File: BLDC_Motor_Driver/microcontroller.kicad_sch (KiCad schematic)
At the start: 27 parts, among them J101 USB4105-GF-A, J102 Conn_01x05, SW101 SW_Push, SW102 SW_Push, U103 STM32L412CBTx, U105 ECMF02-2AMX6

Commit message: finished power circuitry
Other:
- company: (none) -> University of Illinois Urbana-Champaign
- title: (none) -> BLDC Motor Inverter Microcontroller Circuitry
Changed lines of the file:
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@@
 	(generator_version "9.0")
 	(paper "A4")
+	(title_block
+		(title "BLDC Motor Inverter Microcontroller Circuitry")
+		(rev "A")
+		(company "University of Illinois Urbana-Champaign")
+		(comment 4 "Contributors: Thomas McManamen, Noah Breit")
+	)
 	(rectangle
 		(start 93.98 15.24)

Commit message: hall effect done, adding testpoints/connectors
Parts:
- added J601, J602: Conn_01x05, Connector_PinHeader_2.54mm:PinHeader_1x05_P2.54mm_Vertical, symbol Connector_Generic:Conn_01x05
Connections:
- net +3V3: now also J601.1 (Pin_1), J602.1 (Pin_1)
- net GND: now also J601.5 (Pin_5), J602.5 (Pin_5)
- net SPI1_MISO: now also J601.3 (Pin_3)
- net SPI1_MOSI: now also J601.4 (Pin_4)
- net SPI1_SCK: now also J601.2 (Pin_2)
- net SPI2_MISO: now also J602.3 (Pin_3)
- net SPI2_MOSI: now also J602.4 (Pin_4)
- net SPI2_SCK: now also J602.2 (Pin_2)
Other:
- note added: "Connectivity"
- note added: "add others"

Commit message: new GateDriver subsheet. reorg connectors to root sheet
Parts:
- removed C116, C117: 100nF, Capacitor_SMD:C_0603_1608Metric, symbol Device:C
- removed D102: RED LED, LED_SMD:LED_0603_1608Metric, symbol Device:LED
- removed D103: ORANGE LED, LED_SMD:LED_0603_1608Metric, symbol Device:LED
- removed D104: GREEN LED, LED_SMD:LED_0603_1608Metric, symbol Device:LED
- removed D105: BLUE LED, LED_SMD:LED_0603_1608Metric, symbol Device:LED
- removed J101: USB4105-GF-A, Connector_USB:USB_C_Receptacle_GCT_USB4105-xx-A_16P_TopMnt_Horizontal, symbol Connector:USB_C_Receptacle_USB2.0
- removed J102, J601, J602: Conn_01x05, Connector_PinHeader_2.54mm:PinHeader_1x05_P2.54mm_Vertical, symbol Connector_Generic:Conn_01x05
- removed R103: 10k, Resistor_SMD:R_0603_1608Metric, symbol Device:R_US
- removed R104, R105: 5.1k, Resistor_SMD:R_0603_1608Metric, symbol Device:R_US
- removed R107, R108, R109, R110: 470, Resistor_SMD:R_0603_1608Metric, symbol Device:R_US
- removed SW101, SW102: SW_Push, Button_Switch_SMD:SW_SPST_FSMSM, symbol Switch:SW_Push
- removed U105: ECMF02-2AMX6, Package_DFN_QFN:ST_UQFN-6L_1.5x1.7mm_P0.5mm, symbol Power_Protection:ECMF02-2AMX6
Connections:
- net +3V3 renamed 3.3V_REG
- no-connect marks 6 -> 3
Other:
- note removed: "Connectivity"
- note removed: "Debug LEDs"
- note removed: "Power/Serial"
- note removed: "Programming"
- note removed: "USB-C Port"
- note removed: "add others"

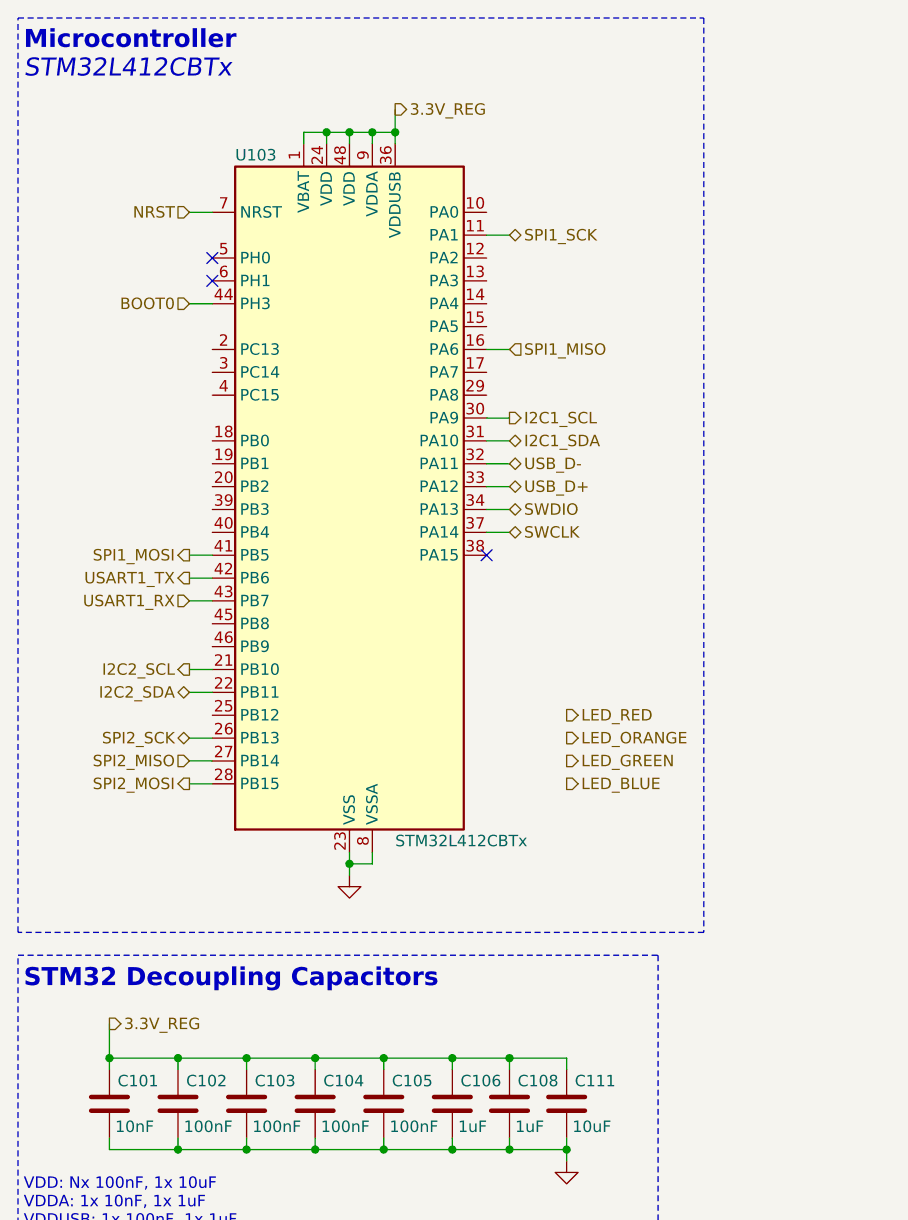
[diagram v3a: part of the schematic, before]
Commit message: added breakout connector and reformatted some things
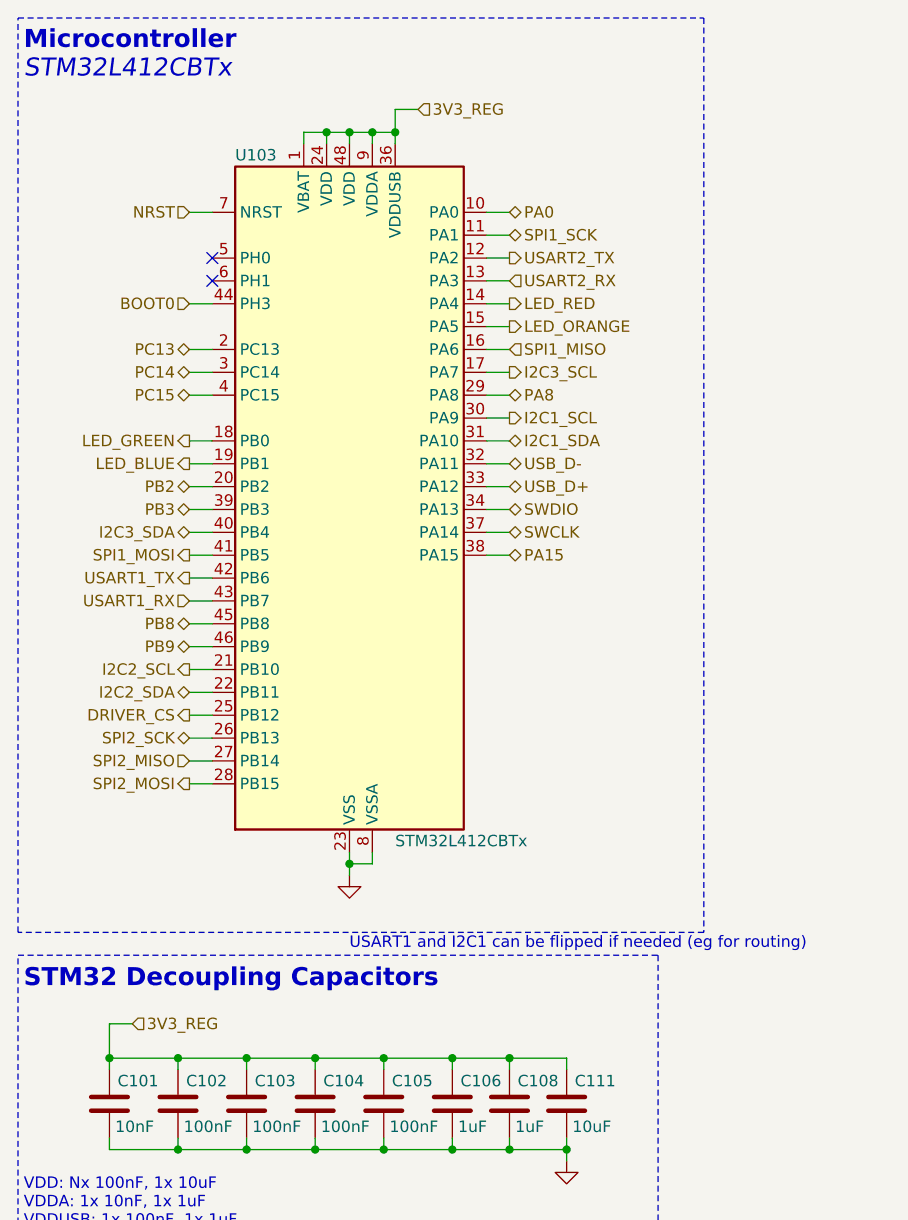
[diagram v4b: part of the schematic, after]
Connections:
- net LED_BLUE: now also U103.19 (PB1)
- net LED_GREEN: now also U103.18 (PB0)
- net LED_ORANGE: now also U103.15 (PA5)
- net LED_RED: now also U103.14 (PA4)
- net PA0: now reaches U103.10 (PA0)
- net USART2_TX: now reaches U103.12 (PA2)
- net USART2_RX: now reaches U103.13 (PA3)
- net I2C3_SCL: now reaches U103.17 (PA7)
- net PC13: now reaches U103.2 (PC13)
- net PB2: now reaches U103.20 (PB2)
- net DRIVER_CS: now reaches U103.25 (PB12)
- net PA8: now reaches U103.29 (PA8)
- net PC14: now reaches U103.3 (PC14)
- net PA15: now reaches U103.38 (PA15)
- net PB3: now reaches U103.39 (PB3)
- net PC15: now reaches U103.4 (PC15)
- net I2C3_SDA: now reaches U103.40 (PB4)
- net PB8: now reaches U103.45 (PB8)
- net PB9: now reaches U103.46 (PB9)
- net 3.3V_REG renamed 3V3_REG
- no-connect marks 3 -> 2
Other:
- note added: "USART1 and I2C1 can be flipped if needed (eg for routing)"

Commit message: schematics more or less done
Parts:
- renumbered C101 to C201, C102 to C202, C103 to C203, C104 to C204, C105 to C205, C106 to C206, C108 to C207, C111 to C208, U103 to U201
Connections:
- net 3V3_REG: no longer U201.1 (VBAT), U201.24 (VDD), U201.36 (VDDUSB), U201.48 (VDD), U201.9 (VDDA)
- new net +3V3: U201.1 (VBAT), U201.24 (VDD), U201.36 (VDDUSB), U201.48 (VDD), U201.9 (VDDA)

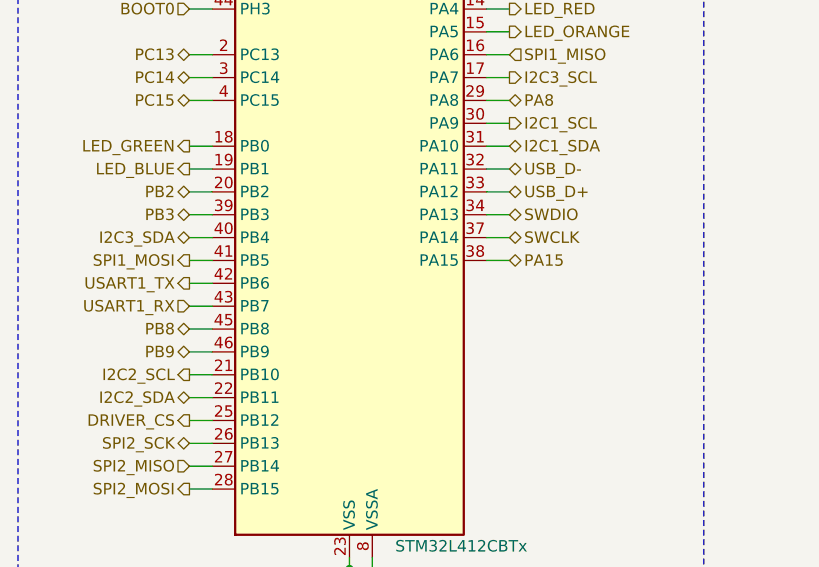
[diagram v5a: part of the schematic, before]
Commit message: wired driver rst/status ios to mcu, layout setup
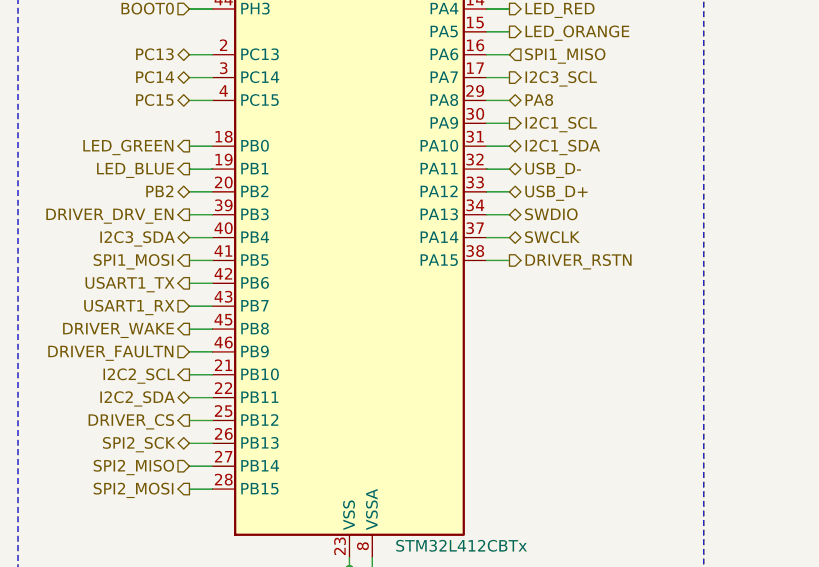
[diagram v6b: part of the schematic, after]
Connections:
- net PA15 renamed DRIVER_RSTN
- net PB3 renamed DRIVER_DRV_EN
- net PB8 renamed DRIVER_WAKE
- net PB9 renamed DRIVER_FAULTN
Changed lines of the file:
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@@
+		)
+	)
+	(hierarchical_label "DRIVER_DRV_EN"
+		(shape output)
+		(at 34.29 69.85 180)
+		(effects
+			(font
+				(size 1.27 1.27)
+			)
+			(justify right)
 		)
 	)
@@
 		)
 	)
-	(hierarchical_label "PB3"
-		(shape bidirectional)
-		(at 34.29 69.85 180)
-		(effects
-			(font
-				(size 1.27 1.27)
-			)
-			(justify right)
-		)
-	)
 	(hierarchical_label "DRIVER_CS"
 		(shape output)
@@
 		)
 	)
+	(hierarchical_label "DRIVER_RSTN"
+		(shape output)
+		(at 69.85 74.93 0)
+		(effects
+			(font
+				(size 1.27 1.27)
+			)
+			(justify left)
+		)
+	)
 	(hierarchical_label "SPI1_MISO"
 		(shape input)
@@
 		)
 	)
-	(hierarchical_label "PB8"
-		(shape bidirectional)
+	(hierarchical_label "DRIVER_FAULTN"
+		(shape input)
+		(at 34.29 85.09 180)
+		(effects
+			(font
+				(size 1.27 1.27)
+			)
+			(justify right)
+		)
+	)
+	(hierarchical_label "PC14"
+		(shape bidirectional)
+		(at 34.29 54.61 180)
+		(effects
+			(font
+				(size 1.27 1.27)
+			)
+			(justify right)
+		)
+	)
+	(hierarchical_label "SPI2_MISO"
+		(shape input)
+		(at 34.29 97.79 180)
+		(effects
+			(font
+				(size 1.27 1.27)
+				(thickness 0.1588)
+			)
+			(justify right)
+		)
+	)
+	(hierarchical_label "SWDIO"
+		(shape bidirectional)
+		(at 69.85 69.85 0)
+		(effects
+			(font
+				(size 1.27 1.27)
+				(thickness 0.1588)
+			)
+			(justify left)
+		)
+	)
+	(hierarchical_label "LED_RED"
+		(shape output)
+		(at 69.85 46.99 0)
+		(effects
+			(font
+				(size 1.27 1.27)
+			)
+			(justify left)
+		)
+	)
+	(hierarchical_label "LED_GREEN"
+		(shape output)
+		(at 34.29 62.23 180)
+		(effects
+			(font
+				(size 1.27 1.27)
+			)
+			(justify right)
+		)
+	)
+	(hierarchical_label "SPI1_MOSI"
+		(shape output)
+		(at 34.29 74.93 180)
+		(effects
+			(font
+				(size 1.27 1.27)
+				(thickness 0.1588)
+			)
+			(justify right)
+		)
+	)
+	(hierarchical_label "SPI1_SCK"
+		(shape bidirectional)
+		(at 69.85 39.37 0)
+		(effects
+			(font
+				(size 1.27 1.27)
+				(thickness 0.1588)
+			)
+			(justify left)
+		)
+	)
+	(hierarchical_label "PC15"
+		(shape bidirectional)
+		(at 34.29 57.15 180)
+		(effects
+			(font
+				(size 1.27 1.27)
+			)
+			(justify right)
+		)
+	)
+	(hierarchical_label "LED_BLUE"
+		(shape output)
+		(at 34.29 64.77 180)
+		(effects
+			(font
+				(size 1.27 1.27)
+			)
+			(justify right)
+		)
+	)
+	(hierarchical_label "LED_ORANGE"
+		(shape output)
+		(at 69.85 49.53 0)
+		(effects
+			(font
+				(size 1.27 1.27)
+			)
+			(justify left)
+		)
+	)
+	(hierarchical_label "PA0"
+		(shape bidirectional)
+		(at 69.85 36.83 0)
+		(effects
+			(font
+				(size 1.27 1.27)
+				(thickness 0.1588)
+			)
+			(justify left)
+		)
+	)
+	(hierarchical_label "DRIVER_WAKE"
+		(shape output)
 		(at 34.29 82.55 180)
 		(effects
@@
 		)
 	)
-	(hierarchical_label "PC14"
-		(shape bidirectional)
-		(at 34.29 54.61 180)
-		(effects
-			(font
-				(size 1.27 1.27)
-			)
-			(justify right)
-		)
-	)
-	(hierarchical_label "SPI2_MISO"
-		(shape input)
-		(at 34.29 97.79 180)
-		(effects
-			(font
-				(size 1.27 1.27)
-				(thickness 0.1588)
-			)
-			(justify right)
-		)
-	)
-	(hierarchical_label "SWDIO"
-		(shape bidirectional)
-		(at 69.85 69.85 0)
-		(effects
-			(font
-				(size 1.27 1.27)
-				(thickness 0.1588)
-			)
-			(justify left)
-		)
-	)
-	(hierarchical_label "LED_RED"
-		(shape output)
-		(at 69.85 46.99 0)
-		(effects
-			(font
-				(size 1.27 1.27)
-			)
-			(justify left)
-		)
-	)
-	(hierarchical_label "PB9"
-		(shape bidirectional)
-		(at 34.29 85.09 180)
-		(effects
-			(font
-				(size 1.27 1.27)
-			)
-			(justify right)
-		)
-	)
-	(hierarchical_label "LED_GREEN"
-		(shape output)
-		(at 34.29 62.23 180)
-		(effects
-			(font
-				(size 1.27 1.27)
-			)
-			(justify right)
-		)
-	)
-	(hierarchical_label "SPI1_MOSI"
-		(shape output)
-		(at 34.29 74.93 180)
-		(effects
-			(font
-				(size 1.27 1.27)
-				(thickness 0.1588)
-			)
-			(justify right)
-		)
-	)
-	(hierarchical_label "SPI1_SCK"
-		(shape bidirectional)
-		(at 69.85 39.37 0)
-		(effects
-			(font
-				(size 1.27 1.27)
-				(thickness 0.1588)
-			)
-			(justify left)
-		)
-	)
-	(hierarchical_label "PC15"
-		(shape bidirectional)
-		(at 34.29 57.15 180)
-		(effects
-			(font
-				(size 1.27 1.27)
-			)
-			(justify right)
-		)
-	)
-	(hierarchical_label "LED_BLUE"
-		(shape output)
-		(at 34.29 64.77 180)
-		(effects
-			(font
-				(size 1.27 1.27)
-			)
-			(justify right)
-		)
-	)
-	(hierarchical_label "LED_ORANGE"
-		(shape output)
-		(at 69.85 49.53 0)
-		(effects
-			(font
-				(size 1.27 1.27)
-			)
-			(justify left)
-		)
-	)
-	(hierarchical_label "PA0"
-		(shape bidirectional)
-		(at 69.85 36.83 0)
-		(effects
-			(font
-				(size 1.27 1.27)
-				(thickness 0.1588)
-			)
-			(justify left)
-		)
-	)
-	(hierarchical_label "PA15"
-		(shape bidirectional)
-		(at 69.85 74.93 0)
-		(effects
-			(font
-				(size 1.27 1.27)
-				(thickness 0.1588)
-			)
-			(justify left)
-		)
-	)
